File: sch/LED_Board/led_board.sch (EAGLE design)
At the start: 4 parts

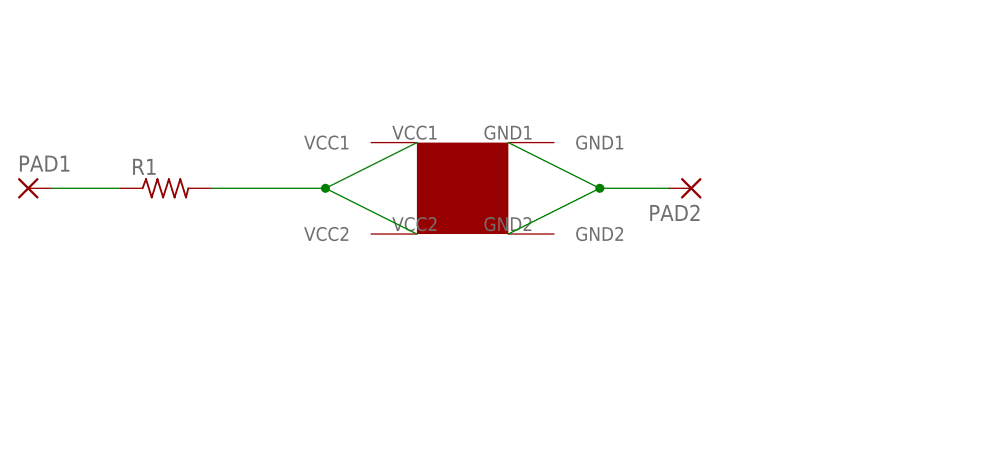
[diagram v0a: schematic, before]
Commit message: More work on schematics.  Using EAGLE exclusively for now... Changed LED board to allow for an attiny4/5/9/10 with a signal pin and to use an RGB led.
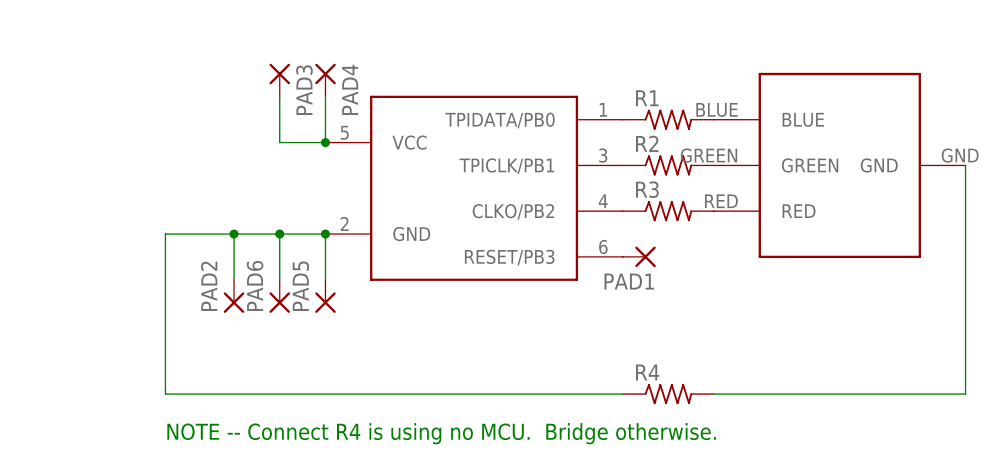
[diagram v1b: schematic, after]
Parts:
- added PAD3, PAD4, PAD5, PAD6: (no value), wirepad:1,6/0,8
- added R2, R3, R4: (no value), resistor:R-US_M1206
- added U$2: ATTINY10SOT, *Personal Library:ATTINY10SOT
- U$1: value 7.6X7.6_LED -> BIVAR-RGB-LED; device MyLib:7.6X7.6_LED -> *Personal Library:BIVAR-RGB-LED
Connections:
- removed net GND: PAD2.P, U$1.GND1, U$1.GND2
- new net N$2: PAD2.P, PAD5.P, PAD6.P, R4.1, U$2.GND
- new net N$3: R2.1, U$2.TPICLK/PB1
- new net N$4: R3.1, U$2.CLKO/PB2
- new net N$5: R1.2, U$1.BLUE
- new net N$6: R2.2, U$1.GREEN
- new net N$7: R3.2, U$1.RED
- new net N$8: R4.2, U$1.GND
- new net N$9: PAD1.P, U$2.RESET/PB3
- net N$1: now also R1.1, U$2.TPIDATA/PB0; no longer R1.2, U$1.VCC1, U$1.VCC2
- net VCC: now also PAD3.P, PAD4.P, U$2.VCC; no longer PAD1.P, R1.1
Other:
- note added: "NOTE -- Connect R4 is using no MCU. Bridge otherwise."
- moved on the sheet: PAD1, PAD2, R1
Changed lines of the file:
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@@
 <?xml version="1.0" encoding="utf-8"?>
 <!DOCTYPE eagle SYSTEM "eagle.dtd">
-<eagle version="5.91">
+<eagle version="6.1">
 <drawing>
 <settings>
@@
 <layer number="19" name="Unrouted" color="6" fill="1" visible="no" active="no"/>
 <layer number="20" name="Dimension" color="15" fill="1" visible="no" active="no"/>
-<layer number="21" name="tPlace" color="7" fill="1" visible="no" active="no"/>
-<layer number="22" name="bPlace" color="7" fill="1" visible="no" active="no"/>
+<layer number="21" name="tPlace" color="16" fill="1" visible="no" active="no"/>
+<layer number="22" name="bPlace" color="14" fill="1" visible="no" active="no"/>
 <layer number="23" name="tOrigins" color="15" fill="1" visible="no" active="no"/>
 <layer number="24" name="bOrigins" color="15" fill="1" visible="no" active="no"/>
@@
 </classes>
 <parts>
-<part name="U$1" library="MyLib" deviceset="7.6X7.6_LED" device=""/>
 <part name="R1" library="resistor" deviceset="R-US_" device="M1206"/>
 <part name="PAD1" library="wirepad" deviceset="1,6/0,8" device=""/>
 <part name="PAD2" library="wirepad" deviceset="1,6/0,8" device=""/>
+<part name="PAD3" library="wirepad" deviceset="1,6/0,8" device=""/>
+<part name="PAD4" library="wirepad" deviceset="1,6/0,8" device=""/>
+<part name="PAD5" library="wirepad" deviceset="1,6/0,8" device=""/>
+<part name="PAD6" library="wirepad" deviceset="1,6/0,8" device=""/>
+<part name="R2" library="resistor" deviceset="R-US_" device="M1206"/>
+<part name="R3" library="resistor" deviceset="R-US_" device="M1206"/>
+<part name="U$1" library="*Personal Library" deviceset="BIVAR-RGB-LED" device=""/>
+<part name="U$2" library="*Personal Library" deviceset="ATTINY10" device="SOT"/>
+<part name="R4" library="resistor" deviceset="R-US_" device="M1206"/>
 </parts>
 <sheets>
 <sheet>
 <plain>
+<text x="-33.02" y="-27.94" size="1.778" layer="91">NOTE -- Connect R4 is using no MCU.  Bridge otherwise.</text>
 </plain>
 <instances>
-<instance part="U$1" gate="G$1" x="0" y="0"/>
-<instance part="R1" gate="G$1" x="-33.02" y="0"/>
-<instance part="PAD1" gate="P" x="-48.26" y="0"/>
-<instance part="PAD2" gate="P" x="25.4" y="0" rot="R180"/>
+<instance part="R1" gate="G$1" x="22.86" y="7.62"/>
+<instance part="PAD1" gate="P" x="20.32" y="-7.62" rot="R180"/>
+<instance part="PAD2" gate="P" x="-25.4" y="-12.7" rot="R90"/>
+<instance part="PAD3" gate="P" x="-20.32" y="12.7" rot="R270"/>
+<instance part="PAD4" gate="P" x="-15.24" y="12.7" rot="R270"/>
+<instance part="PAD5" gate="P" x="-15.24" y="-12.7" rot="R90"/>
+<instance part="PAD6" gate="P" x="-20.32" y="-12.7" rot="R90"/>
+<instance part="R2" gate="G$1" x="22.86" y="2.54"/>
+<instance part="R3" gate="G$1" x="22.86" y="-2.54"/>
+<instance part="U$1" gate="G$1" x="40.64" y="2.54" rot="R180"/>
+<instance part="U$2" gate="G$1" x="0" y="0"/>
+<instance part="R4" gate="G$1" x="22.86" y="-22.86"/>
 </instances>
 <busses>
 </busses>
 <nets>
+<net name="VCC" class="0">
+<segment>
+<wire x1="-20.32" y1="10.16" x2="-20.32" y2="5.08" width="0.1524" layer="91"/>
+<wire x1="-20.32" y1="5.08" x2="-15.24" y2="5.08" width="0.1524" layer="91"/>
+<wire x1="-15.24" y1="5.08" x2="-15.24" y2="10.16" width="0.1524" layer="91"/>
+<pinref part="PAD3" gate="P" pin="P"/>
+<pinref part="PAD4" gate="P" pin="P"/>
+<pinref part="U$2" gate="G$1" pin="VCC"/>
+<junction x="-15.24" y="5.08"/>
+</segment>
+</net>
+<net name="N$2" class="0">
+<segment>
+<pinref part="PAD5" gate="P" pin="P"/>
+<wire x1="-25.4" y1="-5.08" x2="-20.32" y2="-5.08" width="0.1524" layer="91"/>
+<pinref part="PAD6" gate="P" pin="P"/>
+<wire x1="-20.32" y1="-10.16" x2="-20.32" y2="-5.08" width="0.1524" layer="91"/>
+<wire x1="-20.32" y1="-5.08" x2="-15.24" y2="-5.08" width="0.1524" layer="91"/>
+<wire x1="-15.24" y1="-5.08" x2="-15.24" y2="-10.16" width="0.1524" layer="91"/>
+<pinref part="PAD2" gate="P" pin="P"/>
+<wire x1="-25.4" y1="-10.16" x2="-25.4" y2="-5.08" width="0.1524" layer="91"/>
+<wire x1="17.78" y1="-22.86" x2="-33.02" y2="-22.86" width="0.1524" layer="91"/>
+<wire x1="-33.02" y1="-22.86" x2="-33.02" y2="-5.08" width="0.1524" layer="91"/>
+<wire x1="-33.02" y1="-5.08" x2="-25.4" y2="-5.08" width="0.1524" layer="91"/>
+<junction x="-20.32" y="-5.08"/>
+<junction x="-25.4" y="-5.08"/>
+<pinref part="U$2" gate="G$1" pin="GND"/>
+<junction x="-15.24" y="-5.08"/>
+<pinref part="R4" gate="G$1" pin="1"/>
+</segment>
+</net>
+<net name="N$5" class="0">
+<segment>
+<pinref part="R1" gate="G$1" pin="2"/>
+<pinref part="U$1" gate="G$1" pin="BLUE"/>
+</segment>
+</net>
+<net name="N$6" class="0">
+<segment>
+<pinref part="R2" gate="G$1" pin="2"/>
+<pinref part="U$1" gate="G$1" pin="GREEN"/>
+</segment>
+</net>
+<net name="N$7" class="0">
+<segment>
+<pinref part="R3" gate="G$1" pin="2"/>
+<pinref part="U$1" gate="G$1" pin="RED"/>
+</segment>
+</net>
 <net name="N$1" class="0">
 <segment>
-<wire x1="-27.94" y1="0" x2="-15.24" y2="0" width="0.2032" layer="91"/>
-<wire x1="-15.24" y1="0" x2="-5.08" y2="-5.08" width="0.2032" layer="91"/>
-<wire x1="-15.24" y1="0" x2="-5.08" y2="5.08" width="0.2032" layer="91"/>
-<junction x="-15.24" y="0"/>
-<pinref part="U$1" gate="G$1" pin="VCC2"/>
-<pinref part="R1" gate="G$1" pin="2"/>
-<pinref part="U$1" gate="G$1" pin="VCC1"/>
-</segment>
-</net>
-<net name="GND" class="0">
-<segment>
-<wire x1="5.08" y1="5.08" x2="15.24" y2="0" width="0.2032" layer="91"/>
-<wire x1="15.24" y1="0" x2="5.08" y2="-5.08" width="0.2032" layer="91"/>
-<wire x1="15.24" y1="0" x2="22.86" y2="0" width="0.2032" layer="91"/>
-<junction x="15.24" y="0"/>
-<pinref part="U$1" gate="G$1" pin="GND1"/>
-<pinref part="U$1" gate="G$1" pin="GND2"/>
-<pinref part="PAD2" gate="P" pin="P"/>
-</segment>
-</net>
-<net name="VCC" class="0">
-<segment>
-<wire x1="-38.1" y1="0" x2="-45.72" y2="0" width="0.2032" layer="91"/>
 <pinref part="R1" gate="G$1" pin="1"/>
+<pinref part="U$2" gate="G$1" pin="TPIDATA/PB0"/>
+</segment>
+</net>
+<net name="N$3" class="0">
+<segment>
+<pinref part="R2" gate="G$1" pin="1"/>
+<pinref part="U$2" gate="G$1" pin="TPICLK/PB1"/>
+</segment>
+</net>
+<net name="N$4" class="0">
+<segment>
+<pinref part="R3" gate="G$1" pin="1"/>
+<pinref part="U$2" gate="G$1" pin="CLKO/PB2"/>
+</segment>
+</net>
+<net name="N$8" class="0">
+<segment>
+<pinref part="U$1" gate="G$1" pin="GND"/>
+<wire x1="55.88" y1="2.54" x2="55.88" y2="-22.86" width="0.1524" layer="91"/>
+<wire x1="55.88" y1="-22.86" x2="27.94" y2="-22.86" width="0.1524" layer="91"/>
+<pinref part="R4" gate="G$1" pin="2"/>
+</segment>
+</net>
+<net name="N$9" class="0">
+<segment>
+<pinref part="U$2" gate="G$1" pin="RESET/PB3"/>
 <pinref part="PAD1" gate="P" pin="P"/>
 </segment>

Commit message: Added breakout for PB pins on attiny10 on the LED controller.
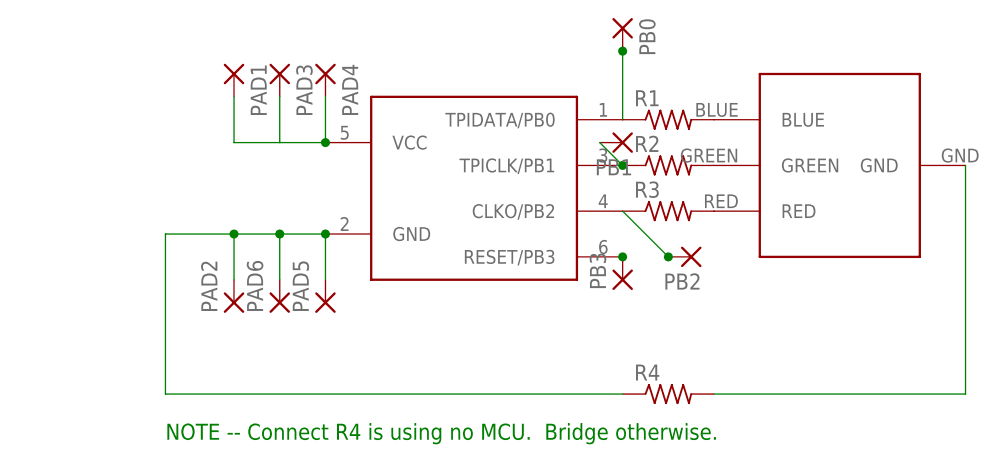
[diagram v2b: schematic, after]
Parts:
- added PB0, PB1, PB2, PB3: (no value), wirepad:1,6/0,8
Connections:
- removed net N$1: R1.1, U$2.TPIDATA/PB0
- removed net N$3: R2.1, U$2.TPICLK/PB1
- removed net N$4: R3.1, U$2.CLKO/PB2
- removed net N$9: PAD1.P, U$2.RESET/PB3
- new net PB0: PB0.P, R1.1, U$2.TPIDATA/PB0
- new net PB1: PB1.P, R2.1, U$2.TPICLK/PB1
- new net PB2: PB2.P, R3.1, U$2.CLKO/PB2
- new net PB3: PB3.P, U$2.RESET/PB3
- net VCC: now also PAD1.P
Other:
- moved on the sheet: PAD1
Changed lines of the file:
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@@
 <parts>
 <part name="R1" library="resistor" deviceset="R-US_" device="M1206"/>
-<part name="PAD1" library="wirepad" deviceset="1,6/0,8" device=""/>
 <part name="PAD2" library="wirepad" deviceset="1,6/0,8" device=""/>
 <part name="PAD3" library="wirepad" deviceset="1,6/0,8" device=""/>
@@
 <part name="U$2" library="*Personal Library" deviceset="ATTINY10" device="SOT"/>
 <part name="R4" library="resistor" deviceset="R-US_" device="M1206"/>
+<part name="PB3" library="wirepad" deviceset="1,6/0,8" device=""/>
+<part name="PB2" library="wirepad" deviceset="1,6/0,8" device=""/>
+<part name="PB1" library="wirepad" deviceset="1,6/0,8" device=""/>
+<part name="PB0" library="wirepad" deviceset="1,6/0,8" device=""/>
+<part name="PAD1" library="wirepad" deviceset="1,6/0,8" device=""/>
 </parts>
 <sheets>
@@
 <instances>
 <instance part="R1" gate="G$1" x="22.86" y="7.62"/>
-<instance part="PAD1" gate="P" x="20.32" y="-7.62" rot="R180"/>
 <instance part="PAD2" gate="P" x="-25.4" y="-12.7" rot="R90"/>
 <instance part="PAD3" gate="P" x="-20.32" y="12.7" rot="R270"/>
@@
 <instance part="U$2" gate="G$1" x="0" y="0"/>
 <instance part="R4" gate="G$1" x="22.86" y="-22.86"/>
+<instance part="PB3" gate="P" x="17.78" y="-10.16" rot="R90"/>
+<instance part="PB2" gate="P" x="25.4" y="-7.62" rot="R180"/>
+<instance part="PB1" gate="P" x="17.78" y="5.08" rot="R180"/>
+<instance part="PB0" gate="P" x="17.78" y="17.78" rot="R270"/>
+<instance part="PAD1" gate="P" x="-25.4" y="12.7" rot="R270"/>
 </instances>
 <busses>
@@
 <pinref part="U$2" gate="G$1" pin="VCC"/>
 <junction x="-15.24" y="5.08"/>
+<pinref part="PAD1" gate="P" pin="P"/>
+<wire x1="-25.4" y1="10.16" x2="-25.4" y2="5.08" width="0.1524" layer="91"/>
+<wire x1="-25.4" y1="5.08" x2="-20.32" y2="5.08" width="0.1524" layer="91"/>
 </segment>
 </net>
@@
 </segment>
 </net>
-<net name="N$1" class="0">
+<net name="PB0" class="0">
 <segment>
 <pinref part="R1" gate="G$1" pin="1"/>
 <pinref part="U$2" gate="G$1" pin="TPIDATA/PB0"/>
+<wire x1="17.78" y1="7.62" x2="17.78" y2="15.24" width="0.1524" layer="91"/>
+<pinref part="PB0" gate="P" pin="P"/>
+<junction x="17.78" y="15.24"/>
 </segment>
 </net>
-<net name="N$3" class="0">
+<net name="PB1" class="0">
 <segment>
 <pinref part="R2" gate="G$1" pin="1"/>
 <pinref part="U$2" gate="G$1" pin="TPICLK/PB1"/>
+<pinref part="PB1" gate="P" pin="P"/>
+<wire x1="15.24" y1="5.08" x2="17.78" y2="2.54" width="0.1524" layer="91"/>
+<junction x="17.78" y="2.54"/>
 </segment>
 </net>
-<net name="N$4" class="0">
+<net name="PB2" class="0">
 <segment>
 <pinref part="R3" gate="G$1" pin="1"/>
 <pinref part="U$2" gate="G$1" pin="CLKO/PB2"/>
+<wire x1="17.78" y1="-2.54" x2="22.86" y2="-7.62" width="0.1524" layer="91"/>
+<pinref part="PB2" gate="P" pin="P"/>
+<junction x="22.86" y="-7.62"/>
 </segment>
 </net>
@@
 </segment>
 </net>
-<net name="N$9" class="0">
+<net name="PB3" class="0">
 <segment>
 <pinref part="U$2" gate="G$1" pin="RESET/PB3"/>
-<pinref part="PAD1" gate="P" pin="P"/>
+<pinref part="PB3" gate="P" pin="P"/>
+<junction x="17.78" y="-7.62"/>
 </segment>
 </net>

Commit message: fixed typo in schematic, removed extra text from board
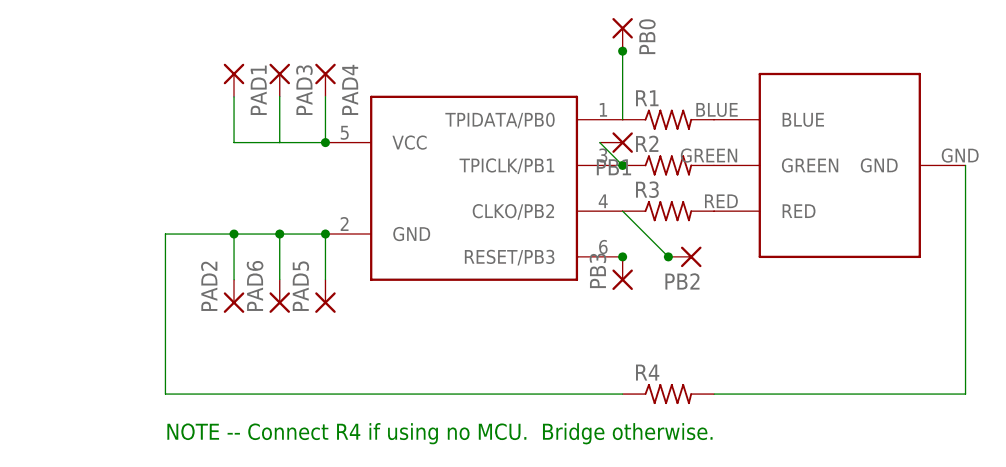
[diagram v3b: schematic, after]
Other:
- note added: "NOTE -- Connect R4 if using no MCU. Bridge otherwise."
- note removed: "NOTE -- Connect R4 is using no MCU. Bridge otherwise."
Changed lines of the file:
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@@
 <sheet>
 <plain>
-<text x="-33.02" y="-27.94" size="1.778" layer="91">NOTE -- Connect R4 is using no MCU.  Bridge otherwise.</text>
+<text x="-33.02" y="-27.94" size="1.778" layer="91">NOTE -- Connect R4 if using no MCU.  Bridge otherwise.</text>
 </plain>
 <instances>
